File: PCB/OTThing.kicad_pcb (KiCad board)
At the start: 2 copper layers, 51.5 x 71 mm, 106 parts, among them IC1 TPS61041, J3 USB_C_Receptacle_USB2.0, K1 G6K-2F-Y-5V, Q1 BC857C, Q10 BC847C, Q11 BC857C, Q12 BC847C, Q13 BC847C, Q2 BC847C, Q4 BC857C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

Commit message: new production
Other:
- board text added: "OT Thing www.seegel-systeme.de 48/25"
- board text removed: "OT Thing www.seegel-systeme.de 15/25"

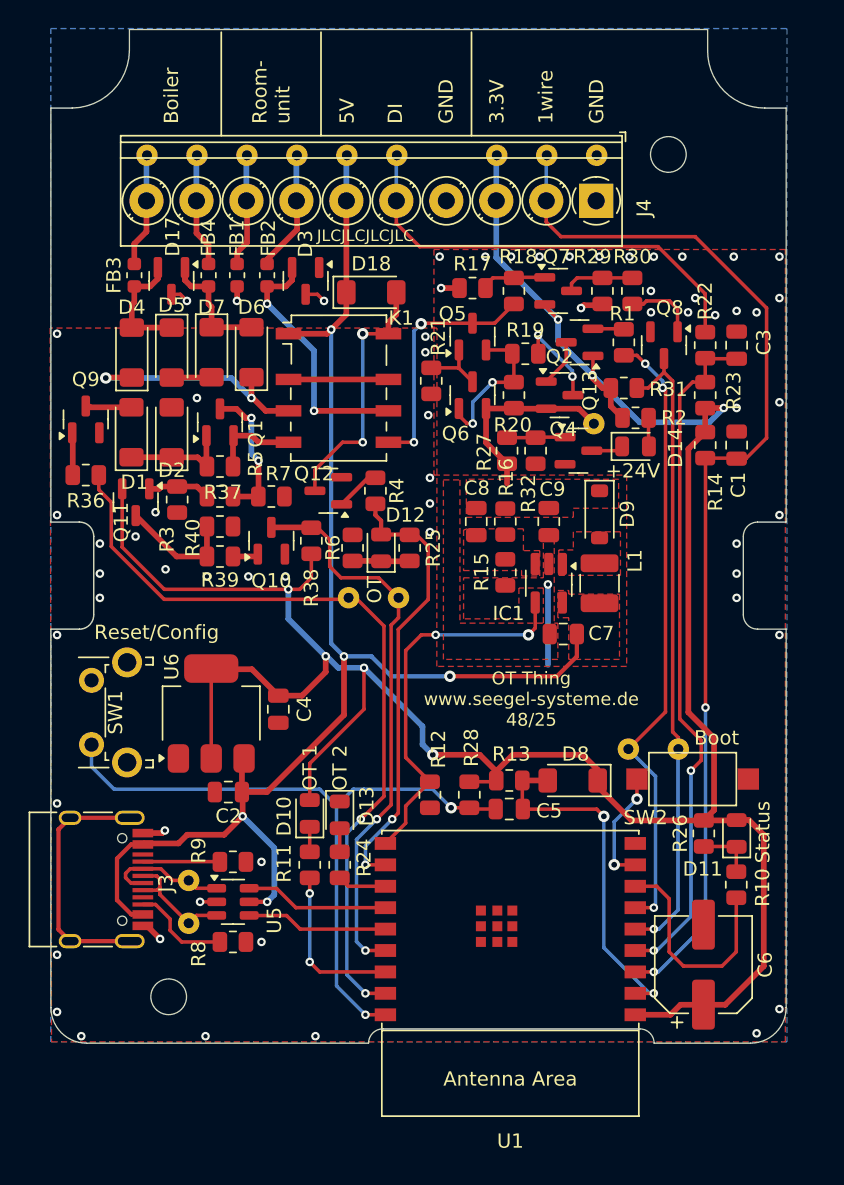
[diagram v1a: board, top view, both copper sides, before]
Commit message: change TVS diodes
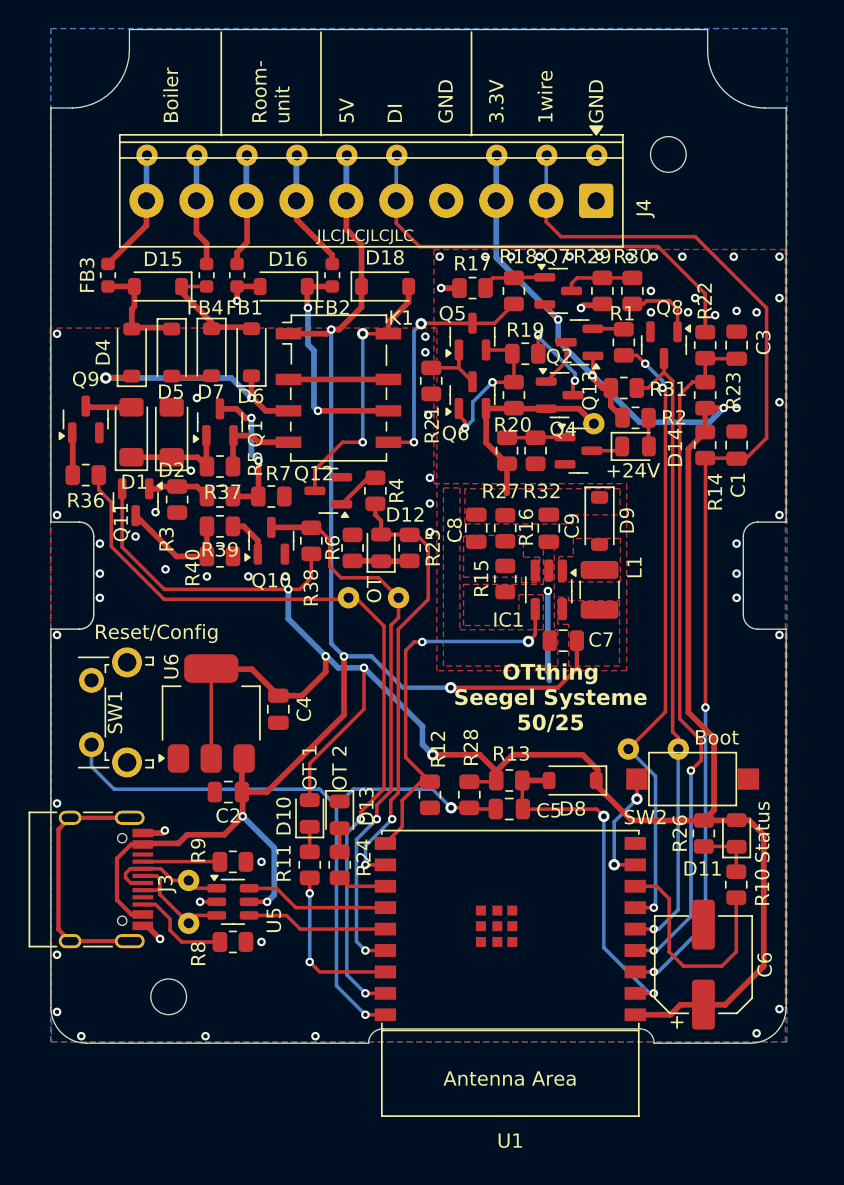
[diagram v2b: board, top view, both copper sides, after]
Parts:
- removed D17, D3: D_Zener_Dual_CommonAnode_KKA_Parallel, Package_TO_SOT_SMD:SOT-23
- added D15: D_TVS, Diode_SMD:D_SOD-123, F.Cu at (122.8, 92.4)
- added D16: D_Schottky, Diode_SMD:D_SOD-123, F.Cu at (131.6, 92.4)
- D18, D4, D5, D6, D7, D8: value LL4148 -> 1N4148W; footprint Diode_SMD:D_MiniMELF -> Diode_SMD:D_SOD-123
- moved FB2 4.56 mm to (135.0, 91.6)
- moved R39 2.11 mm to (127.1, 109.2)
- moved R40 2.09 mm to (127.1, 111.3)
- moved FB3 1.84 mm to (119.3, 91.6)
- moved D18 1.05 mm to (138.7, 92.4)
- moved C7 0.46 mm to (151.2, 117.2)
- moved C8 0.46 mm to (145.1, 109.3)
- moved C9 0.46 mm to (150.2, 109.3)
- moved D9 0.46 mm to (153.7, 108.8)
- moved IC1 0.46 mm to (150.2, 113.7)
- moved L1 0.46 mm to (153.7, 113.7)
- moved R15 0.46 mm to (147.1, 112.9)
- moved R16 0.46 mm to (147.1, 109.3)
- moved FB4 0.14 mm to (126.2, 91.6)
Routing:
- net Net-(D16-K): track 18.1 -> 15.7 mm
- net +5V: track 99.2 -> 101.1 mm
- net Net-(Q10-B): track 1.80 -> 3.11 mm
- net Net-(D15-A2): track 8.41 -> 7.60 mm
- net Net-(D18-A): track 18.1 -> 18.9 mm
- net /OpenTherm interface/OTMASTER_A: track 7.98 -> 8.74 mm
- net +24V: track 13.9 -> 14.6 mm
- net GND: track 19.5 -> 19.0 mm, vias 64 -> 63
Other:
- board text added: "${TITLE} ${COMPANY} ${REVISION}"
- board text removed: "OT Thing www.seegel-systeme.de 48/25"

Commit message: Fix ERCs, DRCs & BOM
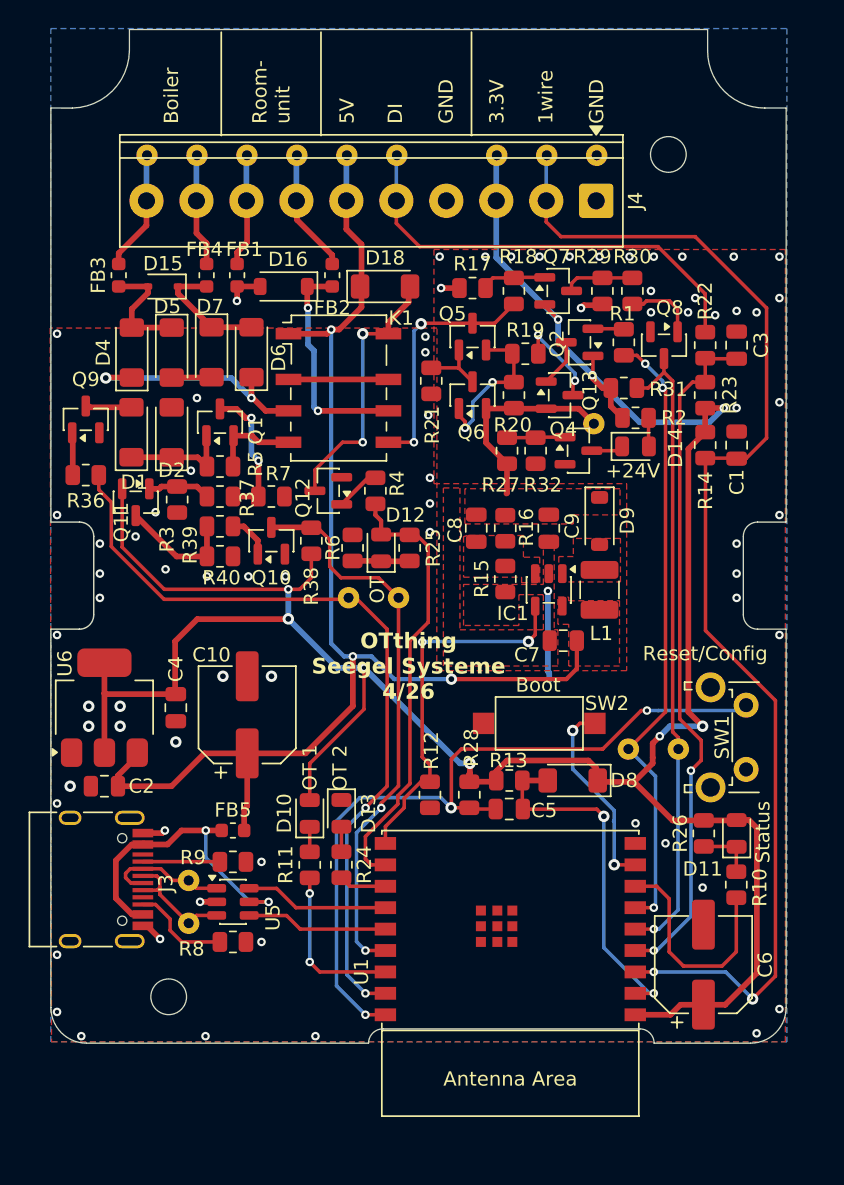
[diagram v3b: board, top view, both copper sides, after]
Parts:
- added C10: 470µ, Capacitor_SMD:CP_Elec_6.3x7.7, F.Cu at (129.0, 122.4)
- added FB5: FerriteBead_Small, Inductor_SMD:L_0603_1608Metric, F.Cu at (128.0, 130.5)
- C2, C4: value 4µ7 -> 10µ
- D15: value D_TVS -> PESD24VL1BA; footprint Diode_SMD:D_SOD-123 -> Diode_SMD:D_SOD-323
- D16: value D_Schottky -> PTVS24VS1UR
- D18, D4, D5, D6, D7, D8: value 1N4148W -> LL4148; footprint Diode_SMD:D_SOD-123 -> Diode_SMD:D_MiniMELF
- FB1, FB2, FB3, FB4: value FerriteBead_Small -> ~
- IC1: footprint Package_TO_SOT_SMD:SOT-23-5_HandSoldering -> Package_TO_SOT_SMD:SOT-23-5
- moved SW1 45.9 mm to (164.0, 121.7), turned to -90 degrees
- moved SW2 11.4 mm to (149.5, 123.0), turned to 180 degrees
- moved C2 8.69 mm to (119.0, 127.4)
- moved U6 7.49 mm to (119.0, 121.9)
- moved C4 7.18 mm to (124.0, 121.9)
- moved FB3 0.75 mm to (120.0, 91.6)
- moved D15 0.35 mm to (123.1, 92.4)
- moved D13 0.16 mm to (135.6, 129.3)
- moved R24 0.12 mm to (135.6, 132.9)
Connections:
- J3 pad A4: +5V -> Net-(U5-VBUS)
- J3 pad A8: unconnected-(J3-SBU1-PadA8) -> (no net)
- J3 pad A9: +5V -> Net-(U5-VBUS)
- J3 pad B4: +5V -> Net-(U5-VBUS)
- J3 pad B8: unconnected-(J3-SBU2-PadB8) -> (no net)
- J3 pad B9: +5V -> Net-(U5-VBUS)
- U5 pad 5: +5V -> Net-(U5-VBUS)
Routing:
- net Net-(U5-VBUS): track 0.00 -> 22.4 mm, vias 0 -> 2
- net unconnected-(J3-SHIELD-PadS1)_2: track 17.7 -> 0.00 mm
- net +5V: track 101.1 -> 90.4 mm, vias 5 -> 3
- net /DQ: track 75.6 -> 86.2 mm
- net Net-(U1-GPIO9): track 8.14 -> 13.9 mm
- net /CFG: track 48.9 -> 53.6 mm, vias 2 -> 3
- net +3.3V: track 182.9 -> 187.2 mm, vias 7 -> 9
- net /EN24: track 27.2 -> 25.9 mm
- net Net-(D15-A1): track 8.41 -> 9.11 mm
- net Net-(D15-A2): track 7.60 -> 8.19 mm
- net /REL: track 31.6 -> 31.2 mm, vias 2 -> 0
- net GND: vias 63 -> 74
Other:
- board text removed: "JLCJLCJLCJLC"

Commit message: update libraries, fix DRCs
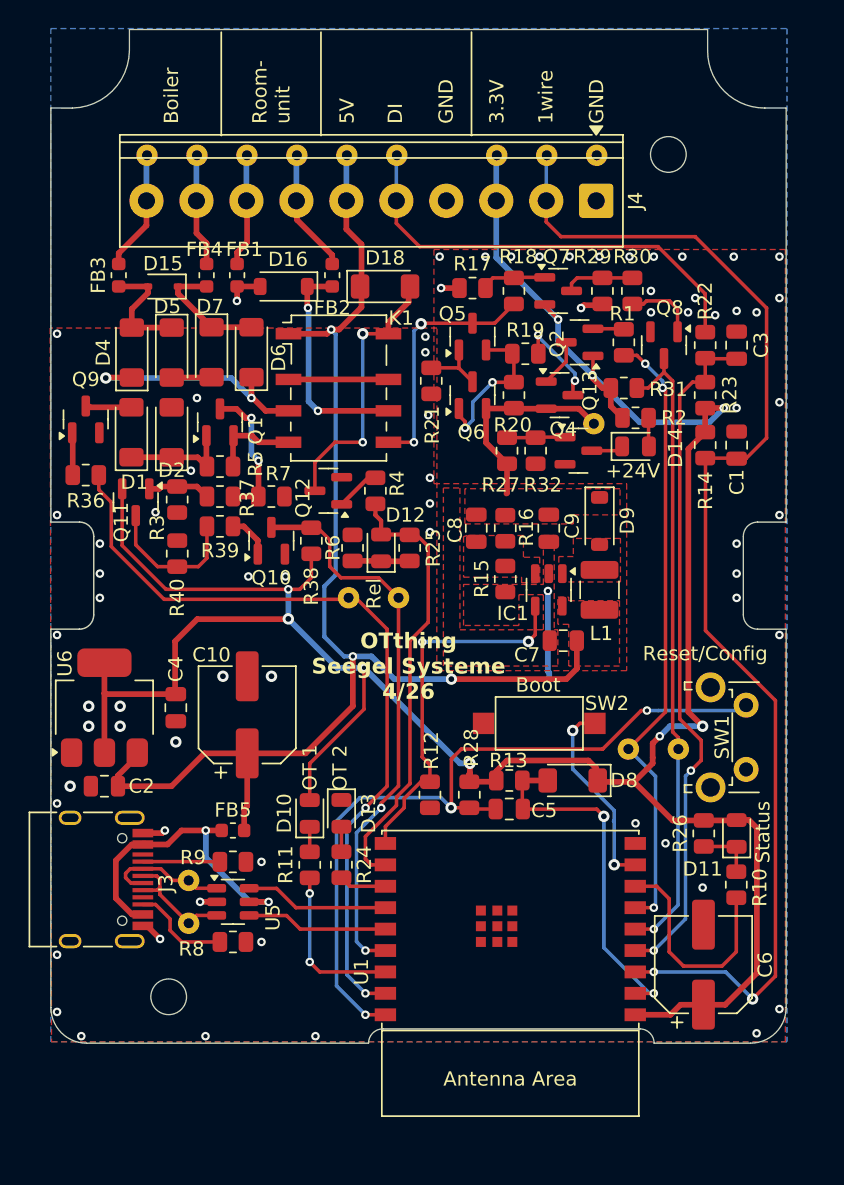
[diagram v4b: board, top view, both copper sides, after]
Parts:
- FB5: value FerriteBead_Small -> ~
- moved R40 3.00 mm to (124.1, 111.1), turned to 90 degrees
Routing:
- net Net-(Q11-C): track 8.27 -> 10.1 mm
- net +5V: track 90.4 -> 91.1 mm
- net GND: vias 74 -> 71
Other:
- board text added: "Rel"
- board text removed: "OT"

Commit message: sensors for flame / pausetime per cycle aux input sensor
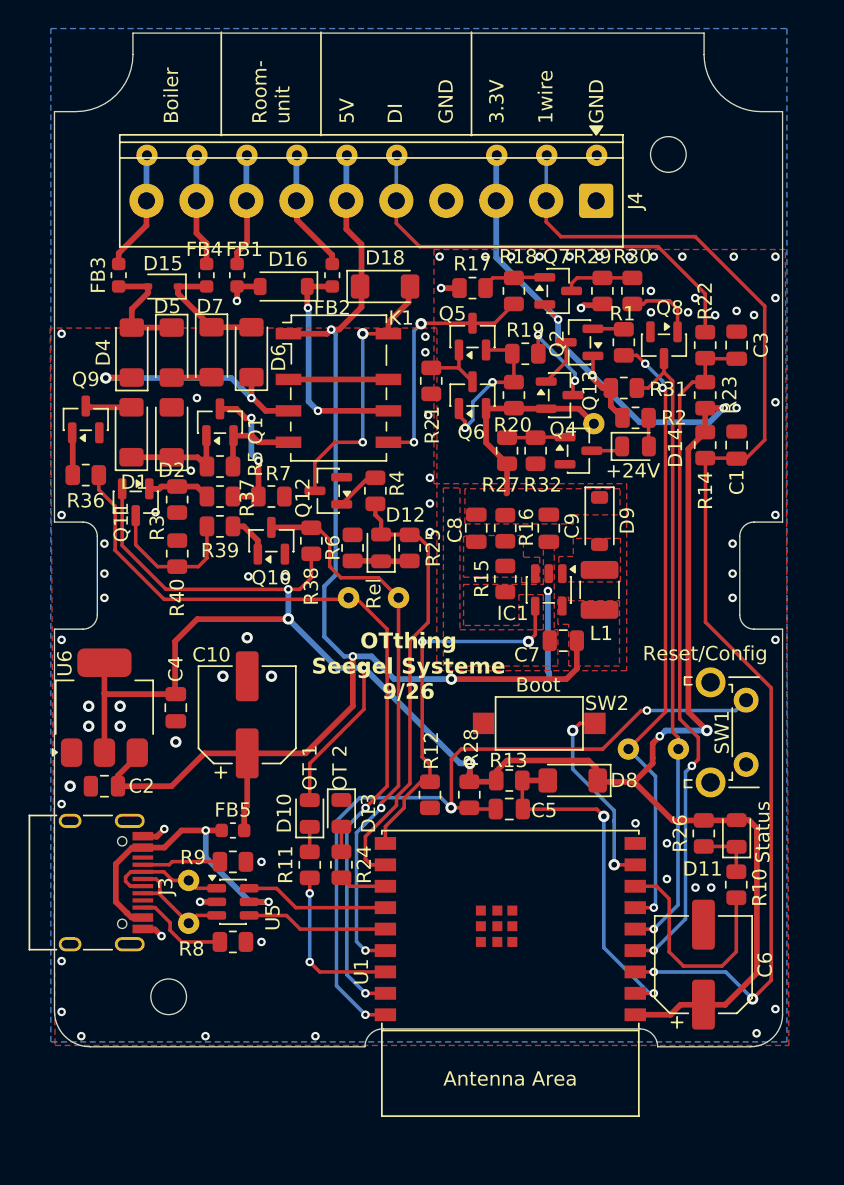
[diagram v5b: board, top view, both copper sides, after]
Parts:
- moved SW1 0.35 mm to (164.0, 121.4)
- moved J3 0.22 mm to (117.7, 134.2)
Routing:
- net +3.3V: track 187.1 -> 187.7 mm
- net GND: vias 71 -> 74
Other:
- board size 51.5 x 71 mm -> 51 x 71 mm

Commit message: fix ERCs & DRCs add TVS diodes to DQ & DI
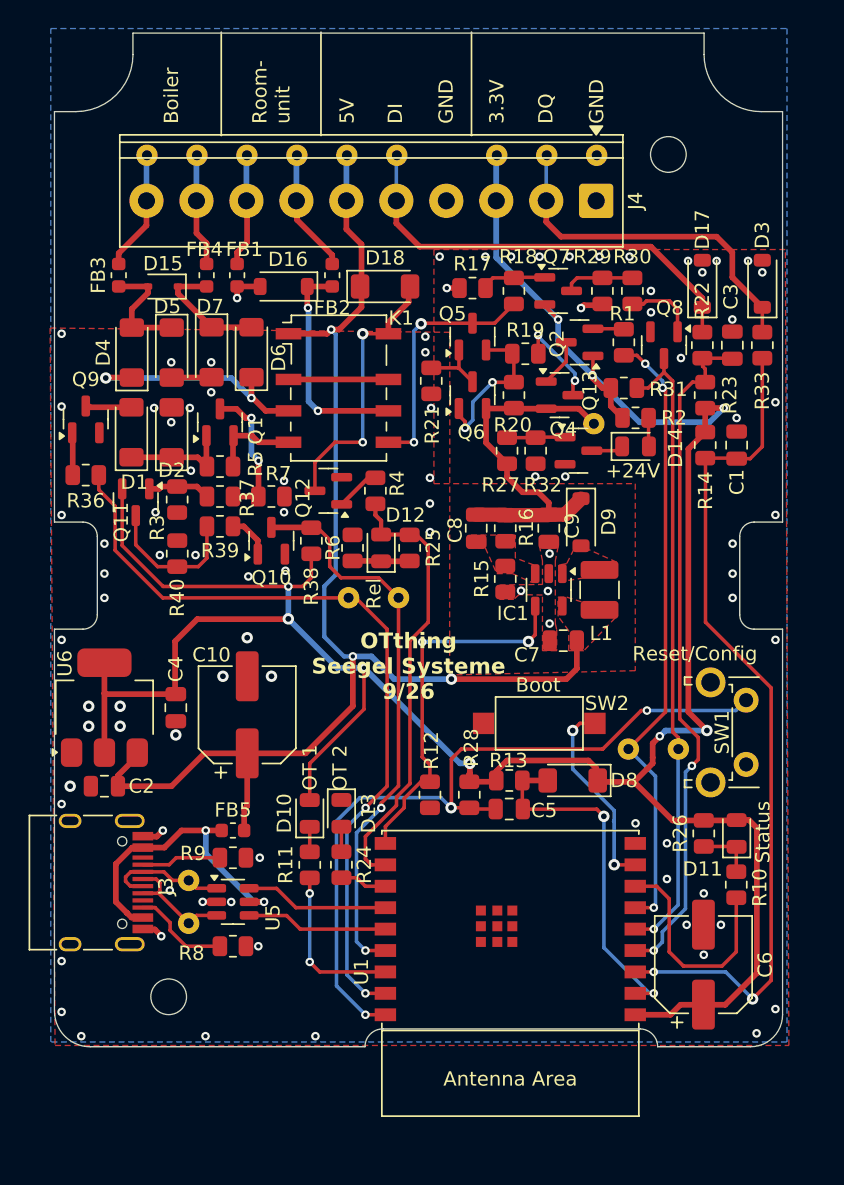
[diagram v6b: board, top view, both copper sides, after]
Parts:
- added D17: PTVS3V3S1UR,115, Diode_SMD:D_SOD-123, F.Cu at (160.9, 92.2)
- added D3: PTVS3V3S1UR,115, Diode_SMD:D_SOD-123, F.Cu at (165.1, 92.2)
- added R33: 330, Resistor_SMD:R_0805_2012Metric, F.Cu at (165.1, 96.5)
- moved D9 1.30 mm to (152.4, 108.9)
- moved R8 0.30 mm to (128.0, 138.6)
- moved C3 0.30 mm to (163.0, 96.5)
- moved R9 0.29 mm to (128.0, 132.4)
- moved R22 0.20 mm to (160.9, 96.5)
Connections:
- net /DM renamed USBDM
- net /DP renamed USBDP
- net /OTM_TX renamed OTM_TX
- net /SW renamed /X2
- net Net-(J3-D+-PadA6) renamed /USBCDP
- net Net-(J3-D--PadA7) renamed /USBCDM
- net Net-(U5-VBUS) renamed +VBUS
- C1 pad 1: /DQ -> Net-(U1-GPIO4/ADC1_CH4)
- J4 pad 2: /DQ -> Net-(D3-K)
- R14 pad 1: /DQ -> Net-(U1-GPIO4/ADC1_CH4)
- TP2 pad 1: /DQ -> Net-(D3-K)
- U1 pad 3: /DQ -> Net-(U1-GPIO4/ADC1_CH4)
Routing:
- net /DQ: track 85.9 -> 0.00 mm, vias 2 -> 0
- net Net-(U1-GPIO4/ADC1_CH4): track 0.00 -> 59.9 mm, vias 0 -> 2
- net Net-(D3-K): track 0.00 -> 25.1 mm
- net +24V: track 14.6 -> 25.7 mm
- net GND: track 19.0 -> 11.8 mm, vias 74 -> 90
- net +VBUS: track 22.4 -> 21.6 mm
- removed copper zone on F.Cu, net +24V
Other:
- board text added: "DQ"
- board text removed: "1wire"

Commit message: add fiducals
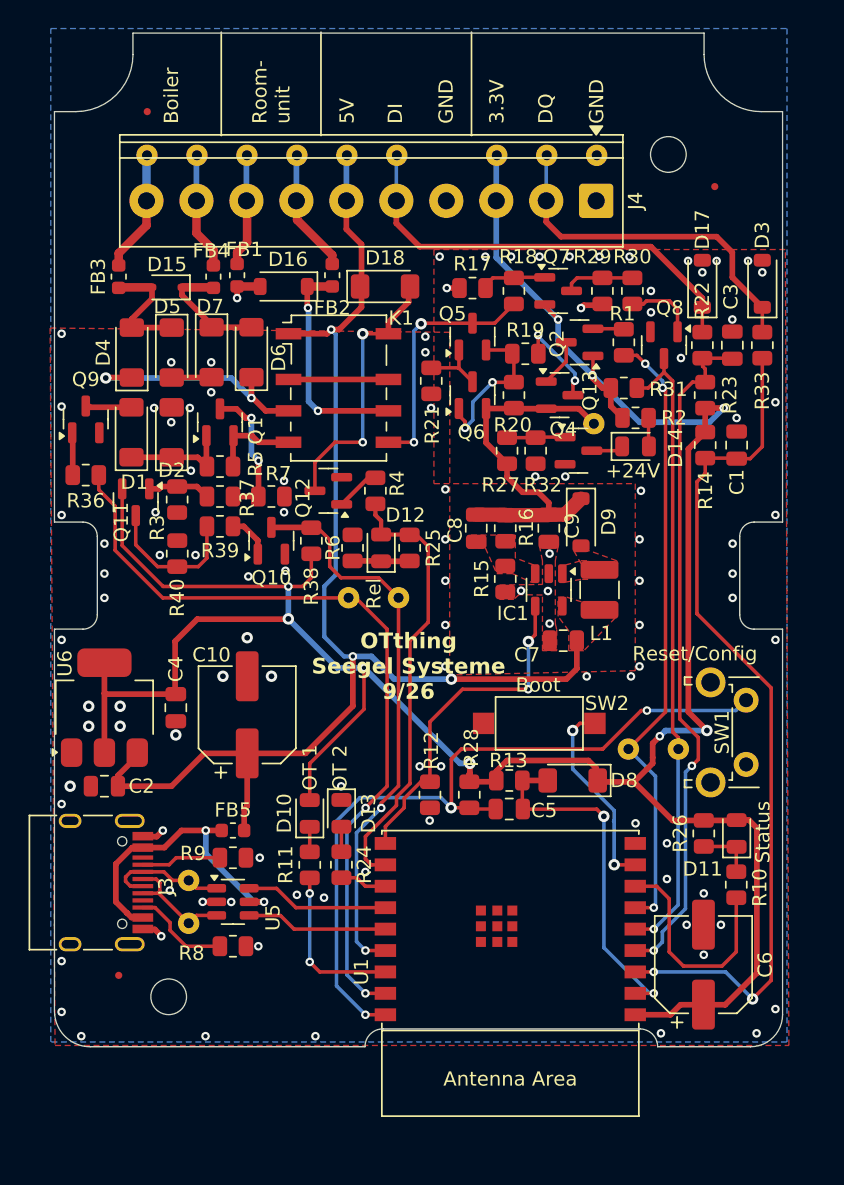
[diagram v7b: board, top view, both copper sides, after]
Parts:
- added FID1: Fiducial, Fiducial:Fiducial_0.5mm_Mask1.5mm, F.Cu at (122.0, 80.2)
- added FID2: Fiducial, Fiducial:Fiducial_0.5mm_Mask1.5mm, F.Cu at (161.8, 85.4)
- added FID3: Fiducial, Fiducial:Fiducial_0.5mm_Mask1.5mm, F.Cu at (120.0, 140.7)
- moved FB4 0.48 mm to (126.7, 91.7)
- moved D15 0.29 mm to (123.4, 92.5)
- moved FB3 0.10 mm to (120.0, 91.7)
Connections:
- net /X2 renamed /DI
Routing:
- net /EN24: track 25.9 -> 23.8 mm
- net GND: vias 90 -> 107
